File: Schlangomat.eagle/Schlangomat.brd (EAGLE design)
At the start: 119 x 85 mm, 41 parts, among them IC1 ULN2003AN, J1 Sensor1, J2 Sensor2, K1 36.11, K2 36.11, K3 36.11, K4 36.11, Q1 16MHz, X1 AC-IN, X2 AC-OUT-1, X3 AC-OUT-2, X4 AC-OUT-3, X5 AC-OUT-4

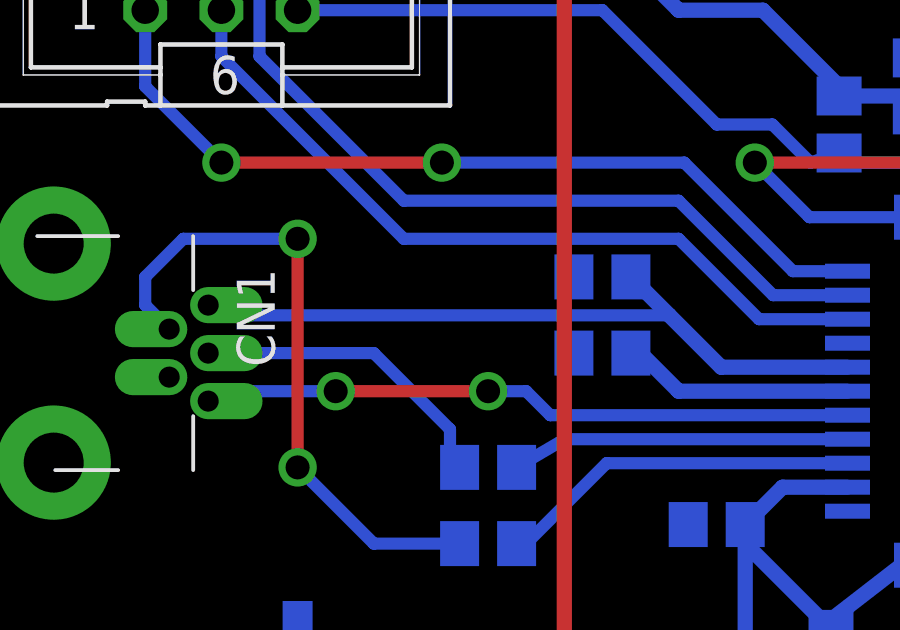
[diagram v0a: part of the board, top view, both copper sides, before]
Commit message: Relaissteuerung und Parser in eigene Files verlagert, allgemeinen Verbesserungen.
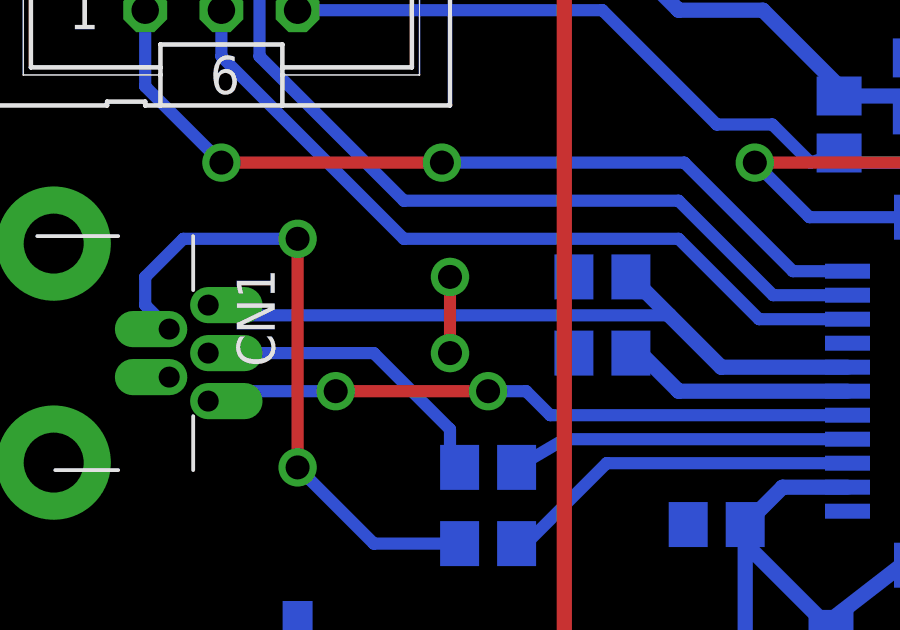
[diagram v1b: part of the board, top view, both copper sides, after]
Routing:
- net GND: track 10.2 -> 12.7 mm, vias 4 -> 6
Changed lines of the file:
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@@
 <via x="42.545" y="59.69" extent="1-16" drill="0.8"/>
 <wire x1="37.465" y1="59.69" x2="42.545" y2="59.69" width="0.508" layer="1"/>
-<wire x1="21.91" y1="33.02" x2="21.91" y2="35.56" width="0" layer="19" extent="16-16"/>
+<via x="17.78" y="35.56" extent="1-16" drill="0.8"/>
+<via x="17.78" y="33.02" extent="1-16" drill="0.8"/>
+<wire x1="17.78" y1="35.56" x2="17.78" y2="33.02" width="0.4064" layer="1"/>
 </signal>
 <signal name="RESET">

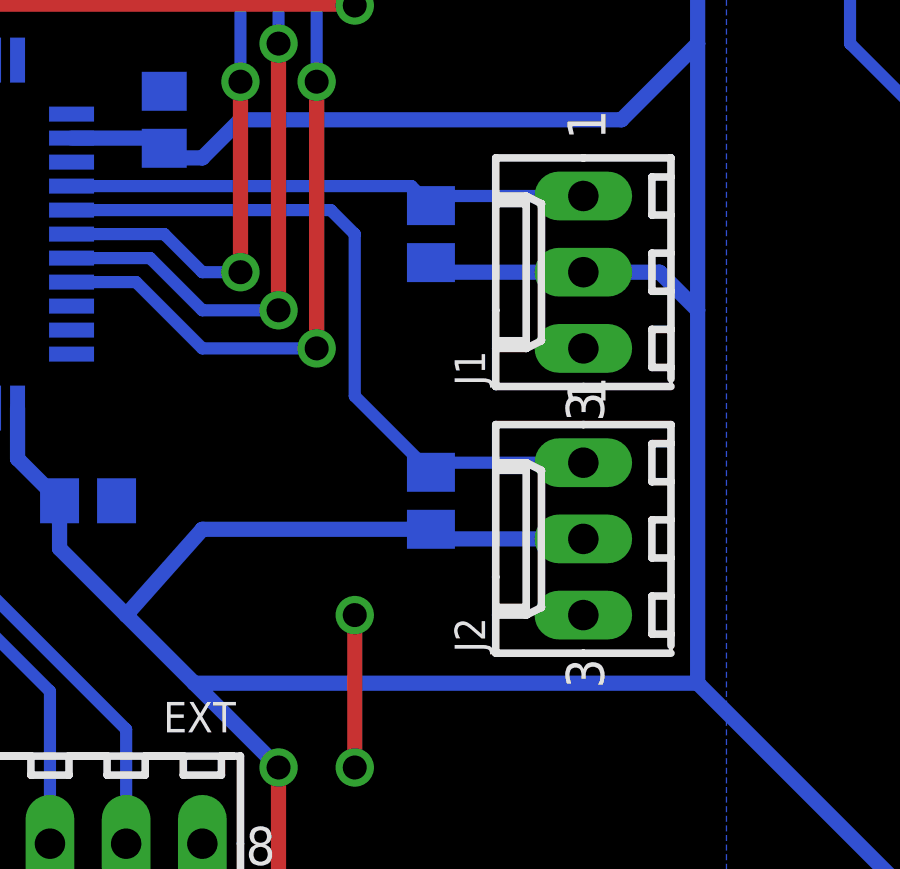
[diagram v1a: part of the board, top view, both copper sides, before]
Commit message: PullUp-FuckUp gefixt, Fehlerbeseitigt
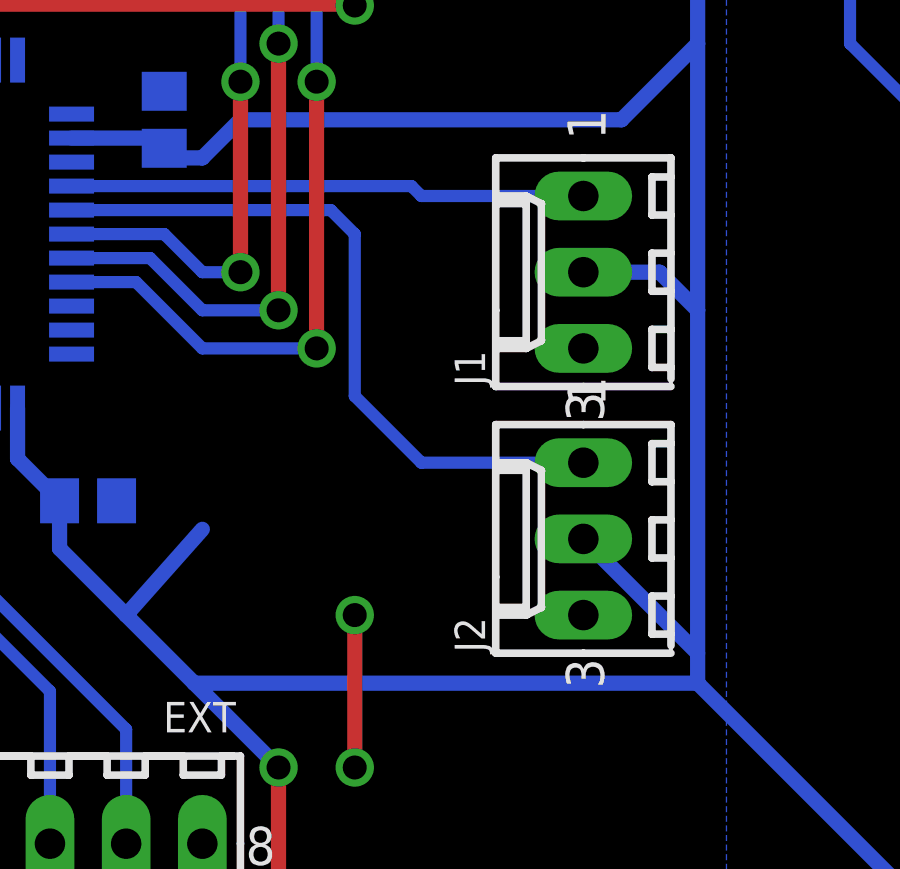
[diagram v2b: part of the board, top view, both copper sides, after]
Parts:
- removed R7, R8: 1K, rcl:M0805
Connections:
- net +5V: no longer R7.2, R8.2
- net SENS1: no longer R8.1
- net SENS2: no longer R7.1
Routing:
- net +5V: track 390.5 -> 378.9 mm
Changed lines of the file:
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@@
 <element name="R5" library="rcl" package="R0805" value="2K" x="40.64" y="74.93" rot="MR270"/>
 <element name="R6" library="rcl" package="R0805" value="10K" x="29.21" y="78.74" rot="MR90"/>
-<element name="R7" library="rcl" package="M0805" value="1K" x="54.61" y="22.86" rot="MR270"/>
-<element name="R8" library="rcl" package="M0805" value="1K" x="54.61" y="31.75" rot="MR270"/>
 <element name="U$1" library="adafruit" package="TQFP44" value="ATMEGA32U4-AU" x="36.83" y="31.75" rot="MR180"/>
 <element name="U$2" library="Zap-Powerconverters" package="TO220V" value="LT1086CT" x="19.05" y="57.15"/>
@@
 <via x="17.78" y="33.02" extent="1-16" drill="0.8"/>
 <wire x1="17.78" y1="35.56" x2="17.78" y2="33.02" width="0.4064" layer="1"/>
+<wire x1="59.69" y1="27.94" x2="59.69" y2="19.05" width="0" layer="19" extent="1-1"/>
 </signal>
 <signal name="RESET">
@@
 <contactref element="J1" pad="2"/>
 <contactref element="J2" pad="2"/>
-<contactref element="R8" pad="2"/>
-<contactref element="R7" pad="2"/>
 <contactref element="POWER" pad="1"/>
 <contactref element="C8" pad="+"/>
@@
 <contactref element="C11" pad="1"/>
 <wire x1="27.62" y1="26.67" x2="30.48" y2="23.81" width="0.508" layer="16"/>
-<wire x1="59.69" y1="21.59" x2="54.93" y2="21.59" width="0.508" layer="16"/>
-<wire x1="54.93" y1="21.59" x2="54.61" y2="21.91" width="0.508" layer="16"/>
-<wire x1="59.69" y1="30.48" x2="54.93" y2="30.48" width="0.508" layer="16"/>
-<wire x1="54.93" y1="30.48" x2="54.61" y2="30.8" width="0.508" layer="16"/>
 <wire x1="34.43" y1="37.55" x2="34.43" y2="40.4175" width="0.508" layer="16"/>
 <wire x1="34.43" y1="40.4175" x2="33.29" y2="40.96" width="0.508" layer="16"/>
@@
 <wire x1="21.59" y1="50.48" x2="21.27" y2="50.8" width="0.508" layer="16"/>
 <wire x1="44.45" y1="19.05" x2="46.99" y2="21.91" width="0.508" layer="16"/>
-<wire x1="46.99" y1="21.91" x2="54.61" y2="21.91" width="0.508" layer="16"/>
 <wire x1="31.03" y1="28.55" x2="28.865" y2="28.55" width="0.508" layer="16"/>
 <wire x1="28.865" y1="28.55" x2="27.62" y2="27.305" width="0.508" layer="16"/>
@@
 <via x="49.53" y="8.89" extent="1-16" drill="0.8"/>
 <wire x1="49.53" y1="8.89" x2="48.26" y2="7.62" width="0.508" layer="16"/>
+<wire x1="63.5" y1="16.78" x2="63.5" y2="17.78" width="0.4064" layer="16"/>
+<wire x1="63.5" y1="17.78" x2="59.69" y2="21.59" width="0.508" layer="16"/>
 </signal>
 <signal name="N$11">
@@
 <contactref element="U$1" pad="27"/>
 <contactref element="J2" pad="1"/>
-<contactref element="R7" pad="1"/>
-<wire x1="59.69" y1="24.13" x2="54.93" y2="24.13" width="0.4064" layer="16"/>
-<wire x1="54.93" y1="24.13" x2="54.61" y2="23.81" width="0.4064" layer="16"/>
+<wire x1="59.69" y1="24.13" x2="54.29" y2="24.13" width="0.4064" layer="16"/>
 <wire x1="42.63" y1="32.55" x2="51.27" y2="32.55" width="0.4064" layer="16"/>
 <wire x1="51.27" y1="32.55" x2="52.07" y2="31.75" width="0.4064" layer="16"/>
 <wire x1="52.07" y1="31.75" x2="52.07" y2="26.35" width="0.4064" layer="16"/>
-<wire x1="52.07" y1="26.35" x2="54.61" y2="23.81" width="0.4064" layer="16"/>
+<wire x1="54.29" y1="24.13" x2="52.07" y2="26.35" width="0.4064" layer="16"/>
 </signal>
 <signal name="SENS1">
 <contactref element="U$1" pad="26"/>
 <contactref element="J1" pad="1"/>
-<contactref element="R8" pad="1"/>
-<wire x1="59.69" y1="33.02" x2="54.93" y2="33.02" width="0.4064" layer="16"/>
-<wire x1="54.93" y1="33.02" x2="54.61" y2="32.7" width="0.4064" layer="16"/>
+<wire x1="59.69" y1="33.02" x2="54.29" y2="33.02" width="0.4064" layer="16"/>
 <wire x1="42.63" y1="33.35" x2="53.96" y2="33.35" width="0.4064" layer="16"/>
-<wire x1="53.96" y1="33.35" x2="54.61" y2="32.7" width="0.4064" layer="16"/>
+<wire x1="54.29" y1="33.02" x2="53.96" y2="33.35" width="0.4064" layer="16"/>
 </signal>
 <signal name="PF0">
